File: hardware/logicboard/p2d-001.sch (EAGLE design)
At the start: 65 parts, among them IC1 74LS06N, IC2 4066N, IC3 MAX3468CPA, J1 MKR, J10 THS, J11 XLR, J2 GPIO, J3 Vcc, J4 RLY, J5 SPI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

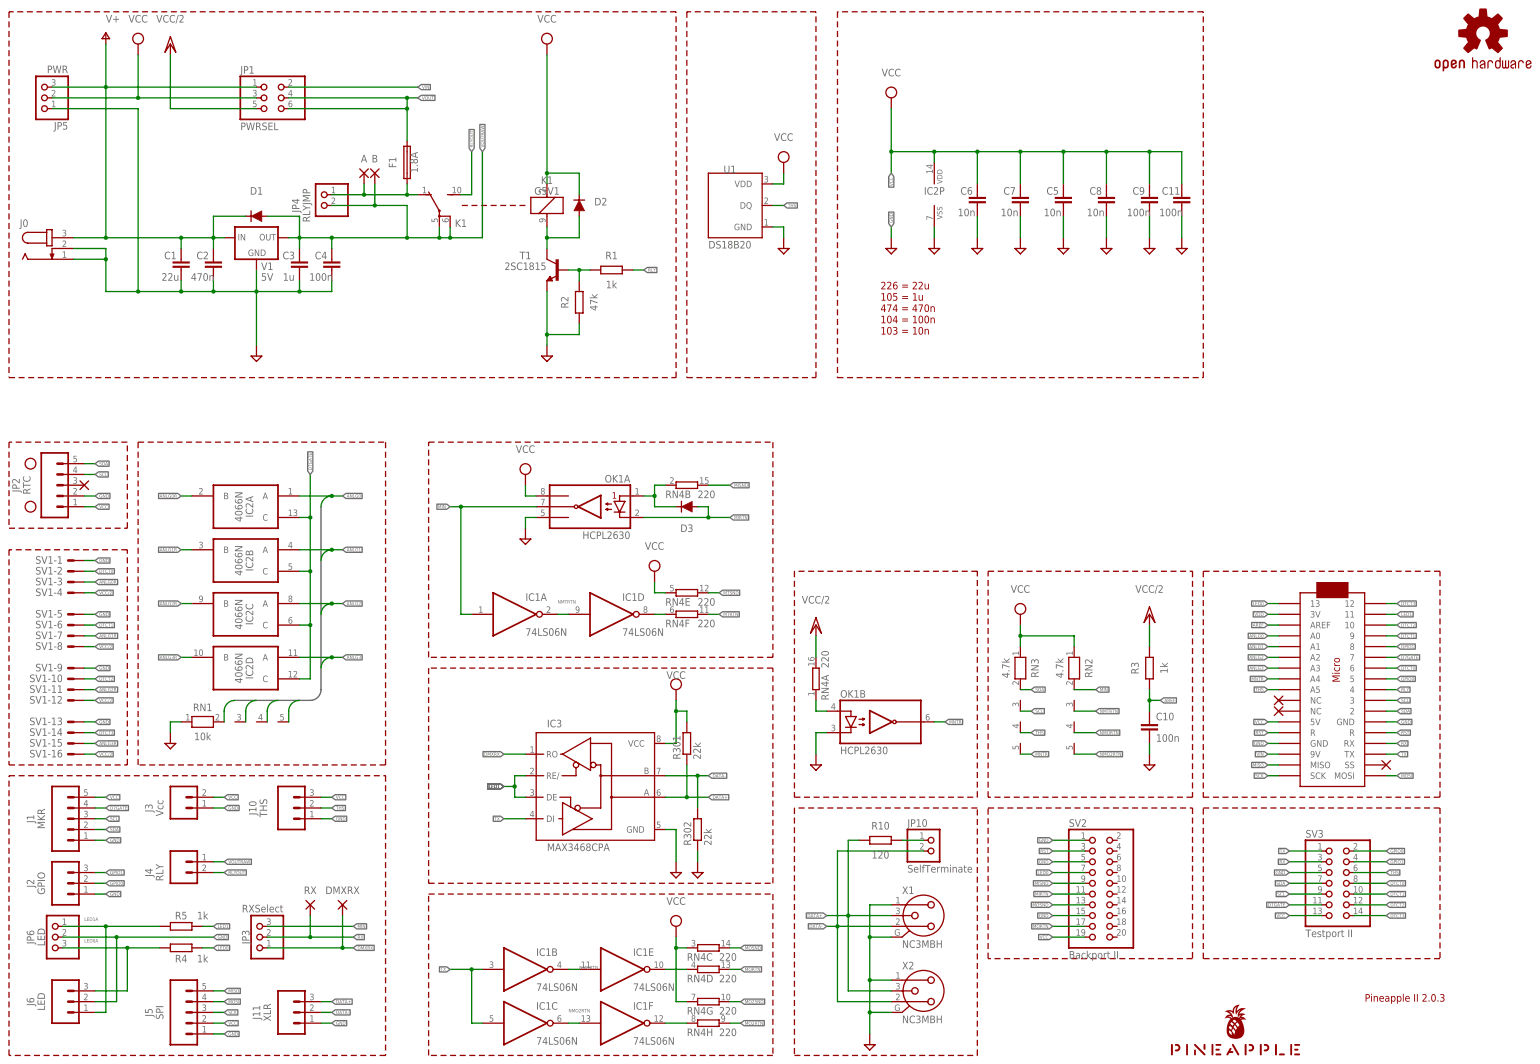
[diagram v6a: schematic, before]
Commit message: Now supports MIDI IN/OUT.
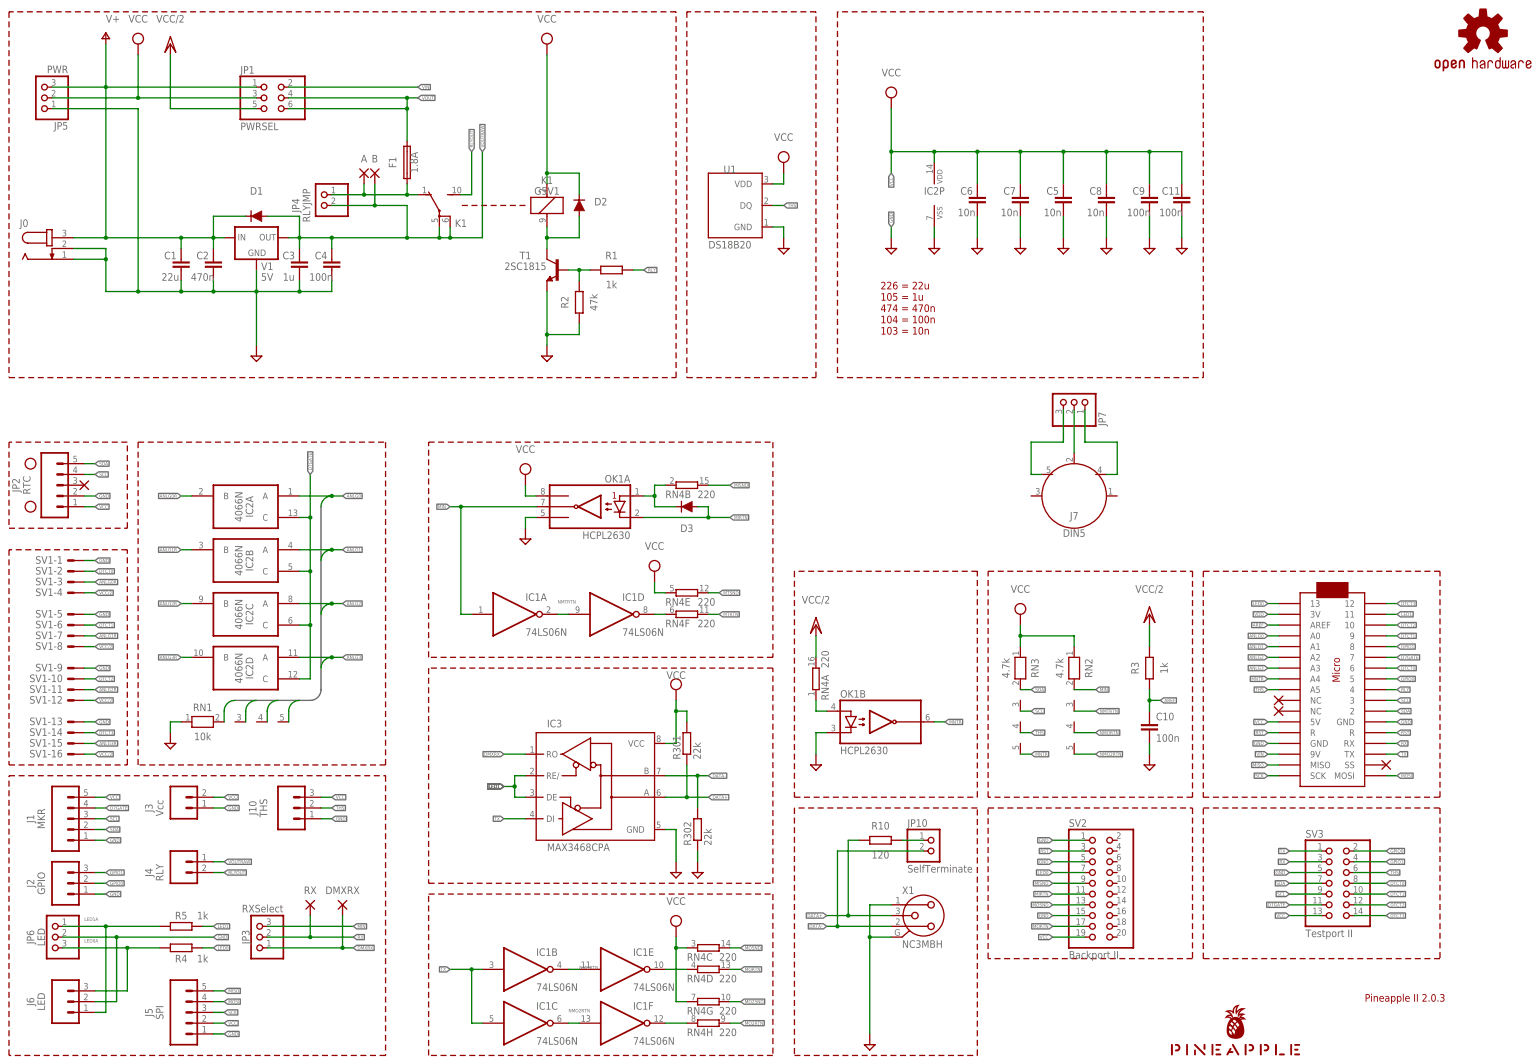
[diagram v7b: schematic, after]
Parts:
- removed J11: XLR, SparkFun-Connectors:CONN_03JST-PTH-VERT
- removed X2: NC3MBH, con-neutrik_ag:NC3MBH
- added J7: DIN5, SparkFun-Connectors:DIN5
- added JP7: (no value), pinhead:PINHD-1X3
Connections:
- new net DIN2: J7.2, JP7.2
- new net DIN4: J7.4, JP7.1
- new net DIN5: J7.5, JP7.3
- net DATA+: no longer J11.3, X2.3
- net DATA-: no longer J11.2, X2.2
- net GND: no longer J11.1, X2.1, X2.G
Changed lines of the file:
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@@
 <part name="J6" library="SparkFun-Connectors" library_urn="urn:adsk.eagle:library:513" deviceset="CONN_03" device="JST-PTH-VERT" package3d_urn="urn:adsk.eagle:package:38080/1" value="LED"/>
 <part name="X1" library="con-neutrik_ag" library_urn="urn:adsk.eagle:library:166" deviceset="NC3" device="MBH" package3d_urn="urn:adsk.eagle:package:8841/1"/>
-<part name="X2" library="con-neutrik_ag" library_urn="urn:adsk.eagle:library:166" deviceset="NC3" device="MBH" package3d_urn="urn:adsk.eagle:package:8841/1"/>
 <part name="IC3" library="maxim" library_urn="urn:adsk.eagle:library:269" deviceset="MAX34*" device="PA" package3d_urn="urn:adsk.eagle:package:29519/2" technology="68C"/>
 <part name="R10" library="resistor" library_urn="urn:adsk.eagle:library:348" deviceset="R-EU_" device="0204/5" package3d_urn="urn:adsk.eagle:package:23488/1" value="120"/>
@@
 <part name="R301" library="rcl" library_urn="urn:adsk.eagle:library:334" deviceset="R-EU_" device="M2012" package3d_urn="urn:adsk.eagle:package:23561/2" value="22k"/>
 <part name="R302" library="rcl" library_urn="urn:adsk.eagle:library:334" deviceset="R-EU_" device="M2012" package3d_urn="urn:adsk.eagle:package:23561/2" value="22k"/>
-<part name="J11" library="SparkFun-Connectors" library_urn="urn:adsk.eagle:library:513" deviceset="CONN_03" device="JST-PTH-VERT" package3d_urn="urn:adsk.eagle:package:38080/1" value="XLR"/>
+<part name="J7" library="SparkFun-Connectors" library_urn="urn:adsk.eagle:library:513" deviceset="DIN5" device="" package3d_urn="urn:adsk.eagle:package:38294/1"/>
+<part name="JP7" library="pinhead" library_urn="urn:adsk.eagle:library:325" deviceset="PINHD-1X3" device="" package3d_urn="urn:adsk.eagle:package:22458/2"/>
 </parts>
 <sheets>
@@
 <attribute name="VALUE" x="233.68" y="33.02" size="1.778" layer="96"/>
 </instance>
-<instance part="X2" gate="G$1" x="238.76" y="22.86" smashed="yes">
-<attribute name="NAME" x="233.68" y="27.94" size="1.778" layer="95"/>
-<attribute name="VALUE" x="233.68" y="15.24" size="1.778" layer="96"/>
-</instance>
 <instance part="IC3" gate="G$1" x="157.48" y="68.58" smashed="yes">
 <attribute name="NAME" x="149.86" y="85.09" size="1.778" layer="95"/>
@@
 <attribute name="VALUE" x="188.722" y="57.15" size="1.778" layer="96" rot="R90"/>
 </instance>
-<instance part="J11" gate="J$1" x="88.9" y="17.78" smashed="yes">
-<attribute name="VALUE" x="83.82" y="17.78" size="1.778" layer="96" rot="R90" align="center"/>
-<attribute name="NAME" x="81.28" y="17.78" size="1.778" layer="95" rot="R90" align="center"/>
+<instance part="J7" gate="G$1" x="274.32" y="139.7" smashed="yes">
+<attribute name="NAME" x="274.32" y="134.112" size="1.778" layer="95" font="vector" align="bottom-center"/>
+<attribute name="VALUE" x="274.32" y="131.826" size="1.778" layer="96" font="vector" align="top-center"/>
+</instance>
+<instance part="JP7" gate="A" x="274.32" y="162.56" smashed="yes" rot="MR90">
+<attribute name="NAME" x="280.035" y="156.21" size="1.778" layer="95" rot="MR90"/>
+<attribute name="VALUE" x="266.7" y="156.21" size="1.778" layer="96" rot="MR90"/>
 </instance>
 </instances>
@@
 <wire x1="226.06" y1="43.18" x2="226.06" y2="35.56" width="0.1524" layer="91"/>
 <pinref part="SUPPLY14" gate="GND" pin="GND"/>
-<pinref part="X2" gate="G$1" pin="1"/>
-<wire x1="226.06" y1="35.56" x2="226.06" y2="25.4" width="0.1524" layer="91"/>
-<wire x1="226.06" y1="25.4" x2="226.06" y2="17.78" width="0.1524" layer="91"/>
-<wire x1="226.06" y1="17.78" x2="226.06" y2="12.7" width="0.1524" layer="91"/>
-<wire x1="231.14" y1="25.4" x2="226.06" y2="25.4" width="0.1524" layer="91"/>
-<junction x="226.06" y="25.4"/>
-<pinref part="X2" gate="G$1" pin="G"/>
-<wire x1="231.14" y1="17.78" x2="226.06" y2="17.78" width="0.1524" layer="91"/>
-<junction x="226.06" y="17.78"/>
+<wire x1="226.06" y1="35.56" x2="226.06" y2="12.7" width="0.1524" layer="91"/>
 <pinref part="X1" gate="G$1" pin="G"/>
 <wire x1="231.14" y1="35.56" x2="226.06" y2="35.56" width="0.1524" layer="91"/>
@@
 <pinref part="SUPPLY22" gate="GND" pin="GND"/>
 <pinref part="R302" gate="G$1" pin="1"/>
-</segment>
-<segment>
-<pinref part="J11" gate="J$1" pin="1"/>
-<wire x1="96.52" y1="15.24" x2="99.06" y2="15.24" width="0.1524" layer="91"/>
-<label x="99.06" y="15.24" size="0.8128" layer="95" xref="yes"/>
 </segment>
 </net>
@@
 <pinref part="X1" gate="G$1" pin="3"/>
 <wire x1="231.14" y1="40.64" x2="220.98" y2="40.64" width="0.1524" layer="91"/>
-<pinref part="X2" gate="G$1" pin="3"/>
 <wire x1="220.98" y1="40.64" x2="215.9" y2="40.64" width="0.1524" layer="91"/>
-<wire x1="231.14" y1="22.86" x2="220.98" y2="22.86" width="0.1524" layer="91"/>
-<wire x1="220.98" y1="22.86" x2="220.98" y2="40.64" width="0.1524" layer="91"/>
 <junction x="220.98" y="40.64"/>
 <label x="215.9" y="40.64" size="0.8128" layer="95" rot="R180" xref="yes"/>
@@
 <pinref part="R301" gate="G$1" pin="1"/>
 </segment>
-<segment>
-<pinref part="J11" gate="J$1" pin="3"/>
-<wire x1="96.52" y1="20.32" x2="99.06" y2="20.32" width="0.1524" layer="91"/>
-<label x="99.06" y="20.32" size="0.8128" layer="95" xref="yes"/>
-</segment>
 </net>
 <net name="DATA-" class="0">
@@
 <pinref part="X1" gate="G$1" pin="2"/>
 <wire x1="231.14" y1="38.1" x2="218.44" y2="38.1" width="0.1524" layer="91"/>
-<pinref part="X2" gate="G$1" pin="2"/>
-<wire x1="218.44" y1="38.1" x2="218.44" y2="20.32" width="0.1524" layer="91"/>
-<wire x1="218.44" y1="20.32" x2="231.14" y2="20.32" width="0.1524" layer="91"/>
 <wire x1="218.44" y1="38.1" x2="215.9" y2="38.1" width="0.1524" layer="91"/>
 <junction x="218.44" y="38.1"/>
@@
 <junction x="185.42" y="73.66"/>
 <pinref part="R302" gate="G$1" pin="2"/>
-</segment>
-<segment>
-<pinref part="J11" gate="J$1" pin="2"/>
-<wire x1="96.52" y1="17.78" x2="99.06" y2="17.78" width="0.1524" layer="91"/>
-<label x="99.06" y="17.78" size="0.8128" layer="95" xref="yes"/>
 </segment>
 </net>
@@
 </segment>
 </net>
+<net name="DIN2" class="0">
+<segment>
+<pinref part="JP7" gate="A" pin="2"/>
+<pinref part="J7" gate="G$1" pin="2"/>
+<wire x1="274.32" y1="160.02" x2="274.32" y2="149.86" width="0.1524" layer="91"/>
+</segment>
+</net>
+<net name="DIN4" class="0">
+<segment>
+<pinref part="JP7" gate="A" pin="1"/>
+<wire x1="276.86" y1="160.02" x2="276.86" y2="152.4" width="0.1524" layer="91"/>
+<wire x1="276.86" y1="152.4" x2="284.48" y2="152.4" width="0.1524" layer="91"/>
+<wire x1="284.48" y1="152.4" x2="284.48" y2="144.78" width="0.1524" layer="91"/>
+<pinref part="J7" gate="G$1" pin="4"/>
+<wire x1="284.48" y1="144.78" x2="281.94" y2="144.78" width="0.1524" layer="91"/>
+</segment>
+</net>
+<net name="DIN5" class="0">
+<segment>
+<pinref part="J7" gate="G$1" pin="5"/>
+<wire x1="266.7" y1="144.78" x2="264.16" y2="144.78" width="0.1524" layer="91"/>
+<wire x1="264.16" y1="144.78" x2="264.16" y2="152.4" width="0.1524" layer="91"/>
+<wire x1="264.16" y1="152.4" x2="271.78" y2="152.4" width="0.1524" layer="91"/>
+<pinref part="JP7" gate="A" pin="3"/>
+<wire x1="271.78" y1="152.4" x2="271.78" y2="160.02" width="0.1524" layer="91"/>
+</segment>
+</net>
